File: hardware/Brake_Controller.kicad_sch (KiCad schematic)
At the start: 13 parts, among them M1 Brake, U4 VNH5200A-E

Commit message: Place and route
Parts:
- removed R18, R19: 3.3k, Resistor_SMD:R_0805_2012Metric_Pad1.20x1.40mm_HandSolder, symbol Device:R_Small_US
- removed U4: VNH5200A-E, Package_SO:SOP-16_3.9x9.9mm_P1.27mm, symbol AMP_Custom:VNH5200A-E
- added U4: VNH7070AS, Package_SO:SOP-16_3.9x9.9mm_P1.27mm, symbol AMP_Custom:VNH7070AS
- C11: footprint Capacitor_SMD:C_Elec_8x10.2 -> Capacitor_THT:CP_Radial_D8.0mm_P3.50mm
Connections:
- net +12V: now also U4.12 (VCC), U4.4 (VCC), U4.5 (VCC)
- net GND: now also U4.1 (GNDA), U4.16 (GNDA), U4.8 (GNDB), U4.9 (GNDB)
- net at R17.1: now also U4.11 (PWM)
- net at R14.2: now also U4.3 (INA)
- net at M1.1 (+): now also U4.15 (OUTA), U4.2 (OUTA)
- net at M1.2 (-): now also U4.10 (OUTB), U4.7 (OUTB)
- net at R16.2: now also U4.14 (SEL0)
- net at R12.1, R13.2: now also U4.13 (CS)
- net at R15.1: now also U4.6 (INB)
- net EN_A renamed SEL0
- net EN_B renamed PWM
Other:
- moved on the sheet: R16, R17

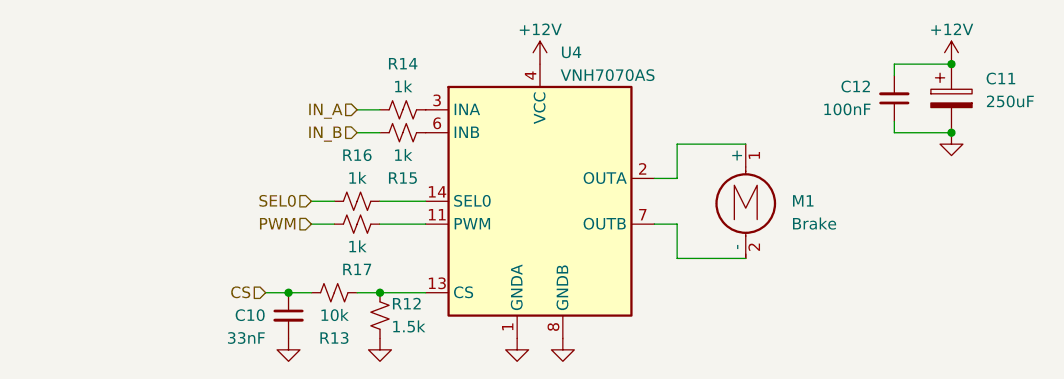
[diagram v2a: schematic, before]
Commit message: Add level shifter for LEDs
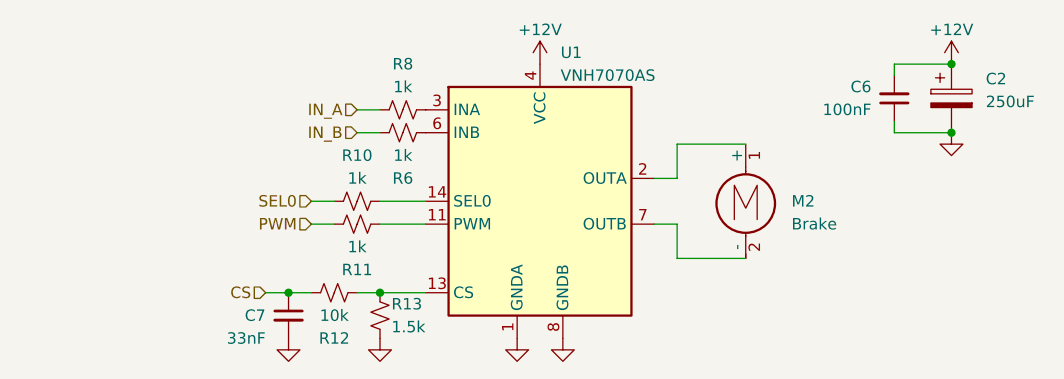
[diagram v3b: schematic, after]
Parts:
- renumbered C11 to C2, C12 to C6, C10 to C7, M1 to M2, R16 to R10, R17 to R11, R13 to R12, R12 to R13, R15 to R6, R14 to R8, U4 to U1
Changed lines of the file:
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@@
 		(on_board yes)
 		(dnp no)
-		(property "Reference" "R14"
+		(property "Reference" "R8"
 			(at 130.81 83.82 90)
 			(effects
@@
 			(project "AMP_PCBv3"
 				(path "/b0eed686-2b97-4c99-952c-ca5393e47dfe/64959e21-8135-46b5-b8e0-be527cd85f0e"
-					(reference "R14")
+					(reference "R8")
 					(unit 1)
 				)
@@
 		(on_board yes)
 		(dnp no)
-		(property "Reference" "R17"
+		(property "Reference" "R11"
 			(at 125.73 106.68 90)
 			(effects
@@
 			(project "AMP_PCBv3"
 				(path "/b0eed686-2b97-4c99-952c-ca5393e47dfe/64959e21-8135-46b5-b8e0-be527cd85f0e"
-					(reference "R17")
+					(reference "R11")
 					(unit 1)
 				)
@@
 		(dnp no)
 		(fields_autoplaced yes)
-		(property "Reference" "M1"
+		(property "Reference" "M2"
 			(at 173.99 99.06 0)
 			(effects
@@
 			(project "AMP_PCBv3"
 				(path "/b0eed686-2b97-4c99-952c-ca5393e47dfe/64959e21-8135-46b5-b8e0-be527cd85f0e"
-					(reference "M1")
+					(reference "M2")
 					(unit 1)
 				)
@@
 		(on_board yes)
 		(dnp no)
-		(property "Reference" "U4"
+		(property "Reference" "U1"
 			(at 148.336 82.55 0)
 			(effects
@@
 			(project "AMP_PCBv3"
 				(path "/b0eed686-2b97-4c99-952c-ca5393e47dfe/64959e21-8135-46b5-b8e0-be527cd85f0e"
-					(reference "U4")
+					(reference "U1")
 					(unit 1)
 				)
@@
 		(on_board yes)
 		(dnp no)
-		(property "Reference" "C12"
+		(property "Reference" "C6"
 			(at 182.88 86.3536 0)
 			(effects
@@
 			(project "AMP_PCBv3"
 				(path "/b0eed686-2b97-4c99-952c-ca5393e47dfe/64959e21-8135-46b5-b8e0-be527cd85f0e"
-					(reference "C12")
+					(reference "C6")
 					(unit 1)
 				)
@@
 		(dnp no)
 		(fields_autoplaced yes)
-		(property "Reference" "C11"
+		(property "Reference" "C2"
 			(at 195.58 85.471 0)
 			(effects
@@
 			(project "AMP_PCBv3"
 				(path "/b0eed686-2b97-4c99-952c-ca5393e47dfe/64959e21-8135-46b5-b8e0-be527cd85f0e"
-					(reference "C11")
+					(reference "C2")
 					(unit 1)
 				)
@@
 		(on_board yes)
 		(dnp no)
-		(property "Reference" "C10"
+		(property "Reference" "C7"
 			(at 115.57 111.76 0)
 			(effects
@@
 			(project "AMP_PCBv3"
 				(path "/b0eed686-2b97-4c99-952c-ca5393e47dfe/64959e21-8135-46b5-b8e0-be527cd85f0e"
-					(reference "C10")
+					(reference "C7")
 					(unit 1)
 				)
@@
 		(on_board yes)
 		(dnp no)
-		(property "Reference" "R15"
+		(property "Reference" "R6"
 			(at 130.81 96.52 90)
 			(effects
@@
 			(project "AMP_PCBv3"
 				(path "/b0eed686-2b97-4c99-952c-ca5393e47dfe/64959e21-8135-46b5-b8e0-be527cd85f0e"
-					(reference "R15")
+					(reference "R6")
 					(unit 1)
 				)
@@
 		(on_board yes)
 		(dnp no)
-		(property "Reference" "R12"
+		(property "Reference" "R13"
 			(at 129.54 110.49 0)
 			(effects
@@
 			(project "AMP_PCBv3"
 				(path "/b0eed686-2b97-4c99-952c-ca5393e47dfe/64959e21-8135-46b5-b8e0-be527cd85f0e"
-					(reference "R12")
+					(reference "R13")
 					(unit 1)
 				)
@@
 		(on_board yes)
 		(dnp no)
-		(property "Reference" "R13"
+		(property "Reference" "R12"
 			(at 123.19 114.3 90)
 			(effects
@@
 			(project "AMP_PCBv3"
 				(path "/b0eed686-2b97-4c99-952c-ca5393e47dfe/64959e21-8135-46b5-b8e0-be527cd85f0e"
-					(reference "R13")
+					(reference "R12")
 					(unit 1)
 				)
@@
 		(on_board yes)
 		(dnp no)
-		(property "Reference" "R16"
+		(property "Reference" "R10"
 			(at 125.73 93.98 90)
 			(effects
@@
 			(project "AMP_PCBv3"
 				(path "/b0eed686-2b97-4c99-952c-ca5393e47dfe/64959e21-8135-46b5-b8e0-be527cd85f0e"
-					(reference "R16")
-					(unit 1)
-				)
+					(reference "R10")
+					(unit 1)
+				)

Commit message: JLC assembly parts
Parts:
- C2: MPN (none) -> A750KS227M1EAAE015; now left out of the parts list
- C6: JLC (none) -> C49678
- C7: JLC (none) -> C1739
- M2: MPN (none) -> 0039281023; now left out of the parts list
- R10, R11, R6, R8: JLC (none) -> C17513
- R12: JLC (none) -> C17414
- R13: JLC (none) -> C4310
- U1: JLC (none) -> C2150622
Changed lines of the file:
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@@
+			)
+		)
+		(property "JLC" "C17513"
+			(at 130.81 88.9 0)
+			(effects
+				(font
+					(size 1.27 1.27)
+				)
+				(hide yes)
 			)
 		)
@@
 			)
 		)
+		(property "JLC" "C17513"
+			(at 125.73 101.6 0)
+			(effects
+				(font
+					(size 1.27 1.27)
+				)
+				(hide yes)
+			)
+		)
 		(pin "2"
 		)
@@
 		(unit 1)
 		(exclude_from_sim no)
-		(in_bom yes)
+		(in_bom no)
 		(on_board yes)
 		(dnp no)
@@
 			)
 		)
+		(property "MPN" "0039281023"
+			(at 168.91 97.79 0)
+			(effects
+				(font
+					(size 1.27 1.27)
+				)
+				(hide yes)
+			)
+		)
 		(pin "1"
 		)
@@
 		(property "Description" "Full Bridge Motor Driver, 41V, 30A, -40 to 150C, MultiPowerSO-30"
 			(at 146.05 125.222 0)
+			(effects
+				(font
+					(size 1.27 1.27)
+				)
+				(hide yes)
+			)
+		)
+		(property "JLC" "C2150622"
+			(at 146.05 99.06 0)
 			(effects
 				(font
@@
 			)
 		)
+		(property "JLC" "C49678"
+			(at 185.42 87.63 0)
+			(effects
+				(font
+					(size 1.27 1.27)
+				)
+				(hide yes)
+			)
+		)
 		(pin "2"
 		)
@@
 		(unit 1)
 		(exclude_from_sim no)
-		(in_bom yes)
+		(in_bom no)
 		(on_board yes)
 		(dnp no)
@@
 			)
 		)
+		(property "MPN" "A750KS227M1EAAE015"
+			(at 191.77 87.63 0)
+			(effects
+				(font
+					(size 1.27 1.27)
+				)
+				(hide yes)
+			)
+		)
 		(pin "2"
 		)
@@
 			)
 		)
+		(property "JLC" "C1739"
+			(at 118.11 111.76 0)
+			(effects
+				(font
+					(size 1.27 1.27)
+				)
+				(hide yes)
+			)
+		)
 		(pin "2"
 		)
@@
 			)
 		)
+		(property "JLC" "C17513"
+			(at 130.81 91.44 0)
+			(effects
+				(font
+					(size 1.27 1.27)
+				)
+				(hide yes)
+			)
+		)
 		(pin "2"
 		)
@@
 			)
 		)
+		(property "JLC" "C4310"
+			(at 128.27 111.76 0)
+			(effects
+				(font
+					(size 1.27 1.27)
+				)
+				(hide yes)
+			)
+		)
 		(pin "2"
 		)
@@
 			)
 		)
+		(property "JLC" "C17414"
+			(at 123.19 109.22 0)
+			(effects
+				(font
+					(size 1.27 1.27)
+				)
+				(hide yes)
+			)
+		)
 		(pin "2"
 		)
@@
 			(at 125.73 99.06 0)
 			(effects
+				(font
+					(size 1.27 1.27)
+				)
+				(hide yes)
+			)
+		)
+		(property "JLC" "C17513"
+			(at 125.73 99.06 0)
+			(effects

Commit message: Schematic cleanup
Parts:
- removed M2: Brake, Connector_Molex:Molex_Mini-Fit_Jr_5566-02A_2x01_P4.20mm_Vertical, symbol Motor:Motor_DC
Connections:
- net OUT_A: now reaches U1.15 (OUTA), U1.2 (OUTA)
- net OUT_B: now reaches U1.10 (OUTB), U1.7 (OUTB)
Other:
- title: Brake Controller -> AMP PCBv3
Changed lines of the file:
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@@
 	(paper "USLetter")
 	(title_block
-		(title "Brake Controller")
-		(date "2024-02-10")
-		(rev "A")
+		(title "AMP PCBv3")
+		(date "2024-04-03")
+		(rev "B")
 		(company "Autonomous Motorsports Purdue")
 	)
@@
 	(wire
 		(pts
-			(xy 161.29 105.41) (xy 161.29 101.6)
-		)
-		(stroke
-			(width 0)
-			(type default)
-		)
-	)
-	(wire
-		(pts
 			(xy 128.27 101.6) (xy 133.35 101.6)
 		)
@@
 	(wire
 		(pts
-			(xy 161.29 96.52) (xy 161.29 92.71)
-		)
-		(stroke
-			(width 0)
-			(type default)
-		)
-	)
-	(wire
-		(pts
 			(xy 128.27 99.06) (xy 133.35 99.06)
 		)
@@
 	(wire
 		(pts
-			(xy 161.29 92.71) (xy 168.91 92.71)
-		)
-		(stroke
-			(width 0)
-			(type default)
-		)
-	)
-	(wire
-		(pts
 			(xy 185.42 90.17) (xy 185.42 91.44)
 		)
@@
 	(wire
 		(pts
-			(xy 168.91 105.41) (xy 161.29 105.41)
-		)
-		(stroke
-			(width 0)
-			(type default)
-		)
-	)
-	(wire
-		(pts
 			(xy 185.42 85.09) (xy 185.42 83.82)
 		)
@@
 		)
 	)
+	(hierarchical_label "OUT_A"
+		(shape input)
+		(at 161.29 96.52 0)
+		(fields_autoplaced yes)
+		(effects
+			(font
+				(size 1.27 1.27)
+			)
+			(justify left)
+		)
+	)
 	(hierarchical_label "SEL0"
 		(shape input)
@@
 			)
 			(justify right)
+		)
+	)
+	(hierarchical_label "OUT_B"
+		(shape input)
+		(at 161.29 101.6 0)
+		(fields_autoplaced yes)
+		(effects
+			(font
+				(size 1.27 1.27)
+			)
+			(justify left)
 		)
 	)
@@
 					(unit 1)
 				)
-			)
-		)
-	)
-	(symbol
-		(lib_id "Motor:Motor_DC")
-		(at 168.91 97.79 0)
-		(unit 1)
-		(exclude_from_sim no)
-		(in_bom no)
-		(on_board yes)
-		(dnp no)
-		(fields_autoplaced yes)
-		(property "Reference" "M2"
-			(at 173.99 99.06 0)
-			(effects
-				(font
-					(size 1.27 1.27)
-				)
-				(justify left)
-			)
-		)
-		(property "Value" "Brake"
-			(at 173.99 101.6 0)
-			(effects
-				(font
-					(size 1.27 1.27)
-				)
-				(justify left)
-			)
-		)
-		(property "Footprint" "Connector_Molex:Molex_Mini-Fit_Jr_5566-02A_2x01_P4.20mm_Vertical"
-			(at 168.91 100.076 0)
-			(effects
-				(font
-					(size 1.27 1.27)
-				)
-				(hide yes)
-			)
-		)
-		(property "Datasheet" "~"
-			(at 168.91 100.076 0)
-			(effects
-				(font
-					(size 1.27 1.27)
-				)
-				(hide yes)
-			)
-		)
-		(property "Description" ""
-			(at 168.91 97.79 0)
-			(effects
-				(font
-					(size 1.27 1.27)
-				)
-				(hide yes)
-			)
-		)
-		(property "MPN" "0039281023"
-			(at 168.91 97.79 0)
-			(effects
-				(font
-					(size 1.27 1.27)
-				)
-				(hide yes)
-			)
-		)
-		(pin "1"
-		)
-		(pin "2"
-		)
-		(instances
-			(project "AMP_PCBv3"
-				(path "/b0eed686-2b97-4c99-952c-ca5393e47dfe/64959e21-8135-46b5-b8e0-be527cd85f0e"
-					(reference "M2")
-					(unit 1)
-				)
